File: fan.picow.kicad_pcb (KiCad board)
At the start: 2 copper layers, 60.3 x 65.7 mm, 53 parts, among them J10 5v Input, J11 12v Input, J12 Temp DHT22, J2 Fan1 Conn, J3 Fan2 Conn, J4 Fan4 Conn, J5 Fan3 Conn, J6 Buzz Conn, J7 OLED, J8 Relay Ctrl, J9 Relay Out, U1 PicoW

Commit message: pop stashed changes
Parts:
- removed J10: 5v Input, Connector_PinHeader_2.54mm:PinHeader_1x02_P2.54mm_Vertical
- removed J11: 12v Input, Connector_PinHeader_2.54mm:PinHeader_1x02_P2.54mm_Vertical
- removed J6: Buzz Conn, Connector_PinHeader_2.54mm:PinHeader_1x03_P2.54mm_Vertical
- removed J8: Relay Ctrl, Connector_PinHeader_2.54mm:PinHeader_1x03_P2.54mm_Vertical
- removed J9: Relay Out, Connector_PinHeader_2.54mm:PinHeader_1x03_P2.54mm_Vertical
- removed JP1: NO/NC Selector, Connector_PinHeader_2.54mm:PinHeader_1x03_P2.54mm_Vertical
- added C10: 0.1uF, Capacitor_SMD:C_0603_1608Metric_Pad1.08x0.95mm_HandSolder, F.Cu at (130.6, 103.1)
- added C11: 10uF, footprints descargados:CL21A106KOQNNNE, F.Cu at (165.4, 65.3)
- added C7: 10pF, Capacitor_SMD:C_0603_1608Metric_Pad1.08x0.95mm_HandSolder, F.Cu at (170.9, 65.3)
- added C8: 1uF, Capacitor_SMD:C_0603_1608Metric_Pad1.08x0.95mm_HandSolder, F.Cu at (168.4, 81.0)
- added D10: 12V, digikey-footprints:0805, F.Cu at (165.4, 89.4)
- added F1: Polyfuse 0.5A, Fuse:Fuse_1206_3216Metric_Pad1.42x1.75mm_HandSolder, F.Cu at (170.9, 62.0)
- added J1: 12v Input, Connector_PinHeader_2.54mm:PinHeader_1x02_P2.54mm_Vertical, F.Cu at (180.7, 82.9)
- added LS1: CMT-7525-80-SMT-TR, footprints descargados:XDCR_CMT-7525-80-SMT-TR, F.Cu at (139.7, 99.1)
- added Q1: AOD4184A, footprints descargados:DPAK228P994X240-4N, F.Cu at (161.8, 104.4)
- added Q2: BSS138, Package_TO_SOT_SMD:SOT-23, F.Cu at (147.3, 96.8)
- added R21: 160k, Resistor_SMD:R_0603_1608Metric_Pad0.98x0.95mm_HandSolder, F.Cu at (165.4, 69.6)
- added R22: 49.9k, Resistor_SMD:R_0603_1608Metric_Pad0.98x0.95mm_HandSolder, F.Cu at (171.9, 89.4)
- added R23: 1k, Resistor_SMD:R_0603_1608Metric_Pad0.98x0.95mm_HandSolder, F.Cu at (152.9, 100.8)
- added SW1: EG1257, footprints descargados:EG1257, F.Cu at (138.0, 108.0)
- added TP1: 5V, TestPoint:TestPoint_Pad_D1.5mm, F.Cu at (165.1, 62.0)
- added TP3: 12V, TestPoint:TestPoint_Pad_D1.5mm, F.Cu at (169.7, 95.0)
- added U2: TLV76701, footprints descargados:TLV76701DGNR, F.Cu at (168.2, 75.8)
- C2: value 0.1uF -> 10uF; footprint Capacitor_SMD:C_0603_1608Metric_Pad1.08x0.95mm_HandSolder -> footprints descargados:CL21A106KOQNNNE
- D1: value LED 12VF -> 12VF; footprint LED_SMD:LED_0805_2012Metric_Pad1.15x1.40mm_HandSolder -> digikey-footprints:0805
- D2, D3, D5, D6: footprint Diode_SMD:D_SMA_Handsoldering -> Diode_SMD:D_SOD-123
- D4: value LED 12V -> 5V; footprint LED_SMD:LED_0805_2012Metric_Pad1.15x1.40mm_HandSolder -> digikey-footprints:0805
- D7: value LED 3V3 -> 3V3; footprint LED_SMD:LED_0805_2012Metric_Pad1.15x1.40mm_HandSolder -> digikey-footprints:0805
- D8: value LED 5V -> ES1D; footprint LED_SMD:LED_0805_2012Metric_Pad1.15x1.40mm_HandSolder -> Diode_SMD:D_1206_3216Metric_Pad1.42x1.75mm_HandSolder
- D9: value 1N5819 -> CDBW140-G; footprint Diode_SMD:D_SMA_Handsoldering -> Diode_SMD:D_SOD-123F
- J12: value Temp DHT22 -> DHT22
- J2: value Fan1 Conn -> Fan1
- J3: value Fan2 Conn -> Fan2
- J4: value Fan4 Conn -> Fan4
- J5: value Fan3 Conn -> Fan3
- R16: value 10K -> 820k
- R8: value 49.9K -> 10k
- TP2: value TestP 3V3 -> 3V3
- moved R1 61.6 mm to (124.5, 46.5), turned to 180 degrees
- moved D1 55.0 mm to (130.0, 46.5), turned to 180 degrees
- moved D4 28.2 mm to (165.4, 56.9), turned to 180 degrees
- moved R8 25.1 mm to (170.9, 56.9), turned to 180 degrees
- moved R15 23.1 mm to (171.4, 52.7)
- moved D8 22.3 mm to (171.4, 84.8)
- moved D7 18.3 mm to (165.3, 52.8)
- moved C6 15.8 mm to (170.2, 44.7)
- moved C5 11.9 mm to (130.0, 50.3)
- moved C4 11.6 mm to (130.3, 62.7)
- moved C3 10.7 mm to (130.3, 75.7)
- moved J12 10.6 mm to (180.8, 56.6)
- moved J7 10.6 mm to (180.9, 68.2)
- moved C1 10.0 mm to (130.6, 88.4)
- moved H3 8.41 mm to (178.8, 106.9)
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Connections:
- C1 pad 2: GND -> /GNDFAN
- C2 pad 1: /12V -> Net-(C2-Pad1)
- C3 pad 2: GND -> /GNDFAN
- C4 pad 2: GND -> /GNDFAN
- C5 pad 2: GND -> /GNDFAN
- D1 pad 1: Net-(D1-Pad1) -> /12V
- D1 pad 2: /12VFAN -> Net-(D1-Pad2)
- D2 pad 1: Net-(D2-Pad1) -> /TACHM1
- D2 pad 2: /TACHM1 -> Net-(D2-Pad2)
- D3 pad 1: Net-(D3-Pad1) -> /TACHM2
- D3 pad 2: /TACHM2 -> Net-(D3-Pad2)
- D4 pad 2: /12V -> GND
- D5 pad 1: Net-(D5-Pad1) -> /TACHM3
- D5 pad 2: /TACHM3 -> Net-(D5-Pad2)
- D6 pad 1: Net-(D6-Pad1) -> /TACHM4
- D6 pad 2: /TACHM4 -> Net-(D6-Pad2)
- D7 pad 1: Net-(D7-Pad1) -> /3V3
- D7 pad 2: /3V3 -> Net-(D7-Pad2)
- D8 pad 1: Net-(D8-Pad1) -> Net-(C2-Pad1)
- D8 pad 2: /VSYS -> /12V
- J2 pad 1: GND -> /GNDFAN
- J2 pad 2: /12VFAN -> /12V
- J3 pad 1: GND -> /GNDFAN
- J3 pad 2: /12VFAN -> /12V
- J4 pad 1: GND -> /GNDFAN
- J4 pad 2: /12VFAN -> /12V
- J5 pad 1: GND -> /GNDFAN
- J5 pad 2: /12VFAN -> /12V
- R1 pad 1: Net-(D1-Pad1) -> Net-(D1-Pad2)
- R1 pad 2: GND -> /GNDFAN
- R10 pad 2: Net-(D5-Pad1) -> Net-(D5-Pad2)
- R11 pad 1: Net-(D5-Pad1) -> Net-(D5-Pad2)
- R11 pad 2: GND -> /GNDFAN
- R12 pad 1: /12VFAN -> /12V
- R13 pad 2: Net-(D6-Pad1) -> Net-(D6-Pad2)
- R14 pad 1: Net-(D6-Pad1) -> Net-(D6-Pad2)
- R14 pad 2: GND -> /GNDFAN
- R15 pad 1: Net-(D7-Pad1) -> Net-(D7-Pad2)
- R16 pad 1: Net-(D8-Pad1) -> Net-(C11-Pad1)
- R16 pad 2: GND -> Net-(C7-Pad2)
- R2 pad 1: /12VFAN -> /12V
- R3 pad 2: Net-(D2-Pad1) -> Net-(D2-Pad2)
- R4 pad 1: Net-(D2-Pad1) -> Net-(D2-Pad2)
- R4 pad 2: GND -> /GNDFAN
- R5 pad 1: /12VFAN -> /12V
- R6 pad 2: Net-(D3-Pad1) -> Net-(D3-Pad2)
- R7 pad 1: Net-(D3-Pad1) -> Net-(D3-Pad2)
- R7 pad 2: GND -> /GNDFAN
- R8 pad 1: Net-(D4-Pad1) -> /5V
- R8 pad 2: GND -> Net-(D4-Pad1)
- R9 pad 1: /12VFAN -> /12V
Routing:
- net /GNDFAN: track 0.00 -> 171.3 mm, vias 0 -> 1
- net /12VFAN: track 151.7 -> 0.00 mm
- net /12V: track 45.3 -> 194.0 mm, vias 2 -> 1
- net GND: track 68.5 -> 132.1 mm, vias 9 -> 2
- net /BUZZ: track 15.3 -> 48.5 mm
- net /3V3: track 136.8 -> 115.1 mm, vias 4 -> 0
- net /5V: track 9.74 -> 31.3 mm, vias 0 -> 2
- net Net-(C11-Pad1): track 0.00 -> 18.3 mm
- net /conectores/NCLOSED: track 16.2 -> 0.00 mm
- net Net-(C2-Pad1): track 0.00 -> 14.7 mm
- net Net-(C7-Pad2): track 0.00 -> 12.7 mm
- net /VSYS: track 29.5 -> 17.3 mm
- net Net-(Q1-Pad1): track 0.00 -> 12.1 mm
- net Net-(D2-Pad2): track 0.00 -> 11.1 mm
- net /TEMPHUM: track 18.7 -> 29.7 mm
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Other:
- board size 60.3 x 65.7 mm -> 73.4 x 70.5 mm
- board text added: "0.2000 mm / 0.0000 mm"
- board text added: "0.3000 mm"
- board text added: "1.6000 mm"
- board text added: "2"
- board text added: "60.2996 mm x 65.6844 mm"
- board text added: "BOARD CHARACTERISTICS"
- board text added: "Board Thickness:"
- board text added: "Board overall dimensions:"
- board text added: "Castellated pads:"
- board text added: "Copper Finish:"
- board text added: "Copper Layer Count:"
- board text added: "Edge card connectors:"
- board text added: "Falta: - Graficos detras - Version de la placa - Iniciales - Tamaño de la placa (para caja standard) y posicion agujeros - Redondear los bordes (cambiar rectangulo por lineas) - Tamaños de los componentes"
- board text added: "Fan Controller v0.1 Based on RaspberryPi PicoW MCU"
- board text added: "Impedance Control:"
- board text added: "Min hole diameter:"
- board text added: "Min track/spacing:"
- board text added: "No"
- board text added: "None"
- board text added: "Plated Board Edge:"
- board text added: "by Jaime Botella jimbotel@gmail.com 2022/11"
- board text removed: "12VF"
- board text removed: "5V"
- board text removed: "Falta: - Graficos detras - Version de la placa - Iniciales - Validar valores Rs de LEDs - Tamaños de los componentes"
- board text removed: "IN"
- board text removed: "NCLSD"
- board text removed: "NOPEN"
- board text removed: "RELC"

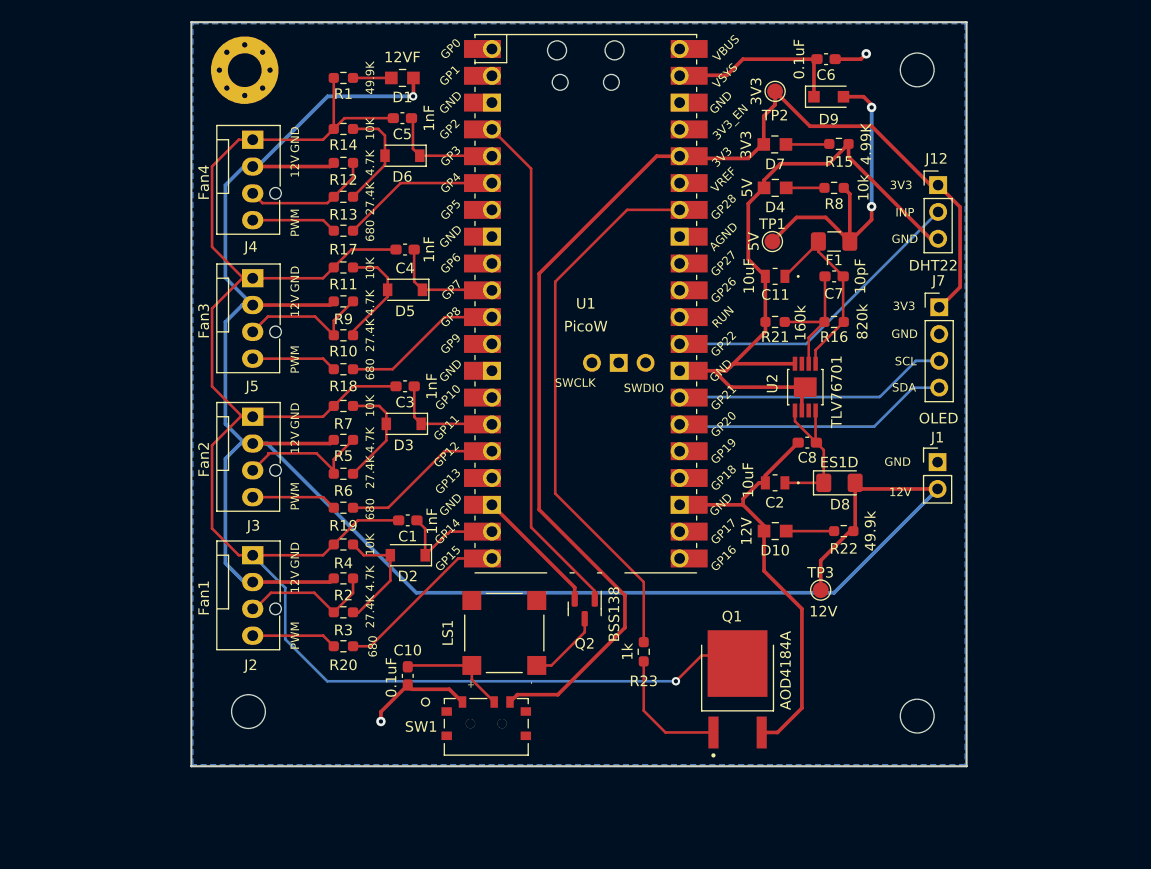
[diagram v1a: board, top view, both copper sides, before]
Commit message: add GNDFAN net to Power netclass
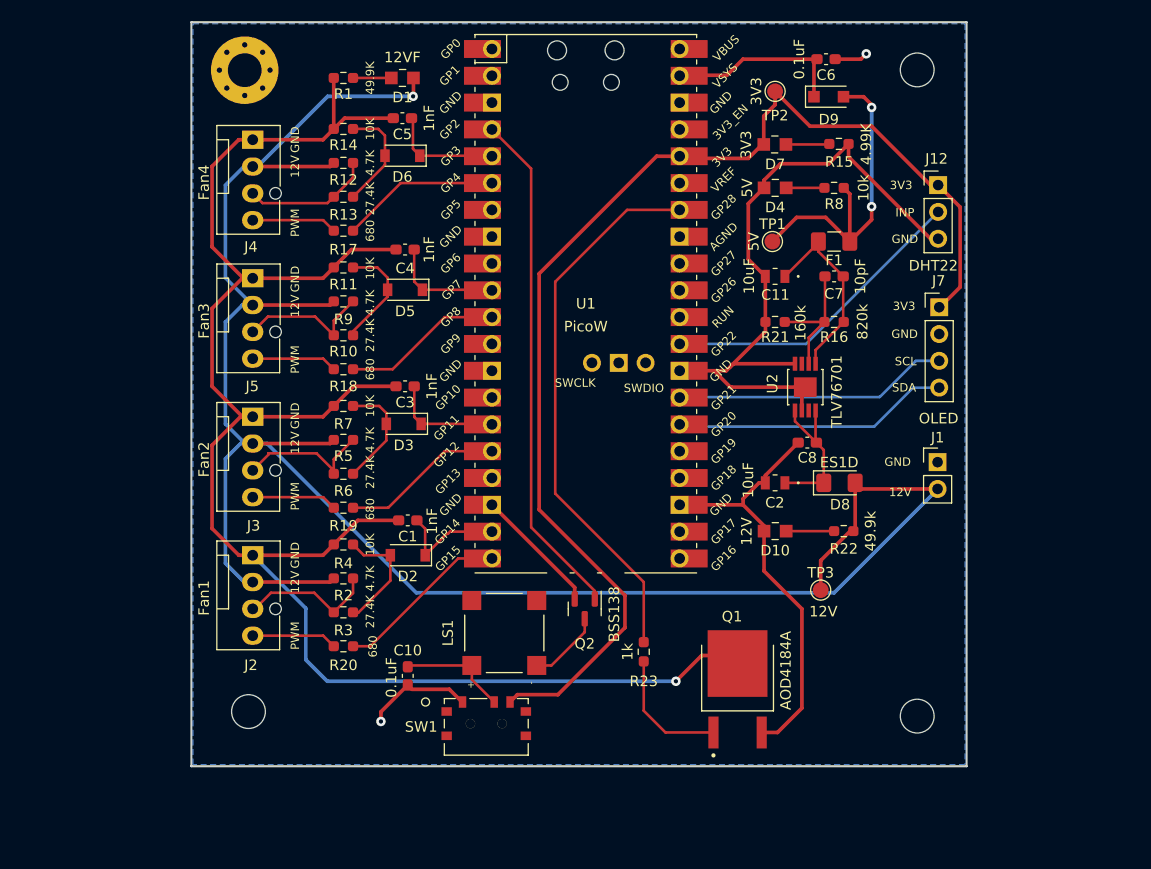
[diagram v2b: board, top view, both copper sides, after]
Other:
- board text added: "Falta: - Tamaño de la placa (para caja standard) y posicion agujeros - Redondear los bordes (cambiar rectangulo por lineas)"
- board text removed: "0.2000 mm / 0.0000 mm"
- board text removed: "0.3000 mm"
- board text removed: "1.6000 mm"
- board text removed: "2"
- board text removed: "60.2996 mm x 65.6844 mm"
- board text removed: "BOARD CHARACTERISTICS"
- board text removed: "Board Thickness:"
- board text removed: "Board overall dimensions:"
- board text removed: "Castellated pads:"
- board text removed: "Copper Finish:"
- board text removed: "Copper Layer Count:"
- board text removed: "Edge card connectors:"
- board text removed: "Falta: - Graficos detras - Version de la placa - Iniciales - Tamaño de la placa (para caja standard) y posicion agujeros - Redondear los bordes (cambiar rectangulo por lineas) - Tamaños de los componentes"
- board text removed: "Impedance Control:"
- board text removed: "Min hole diameter:"
- board text removed: "Min track/spacing:"
- board text removed: "No"
- board text removed: "None"
- board text removed: "Plated Board Edge:"

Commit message: edit some footprints to give more room to the pads
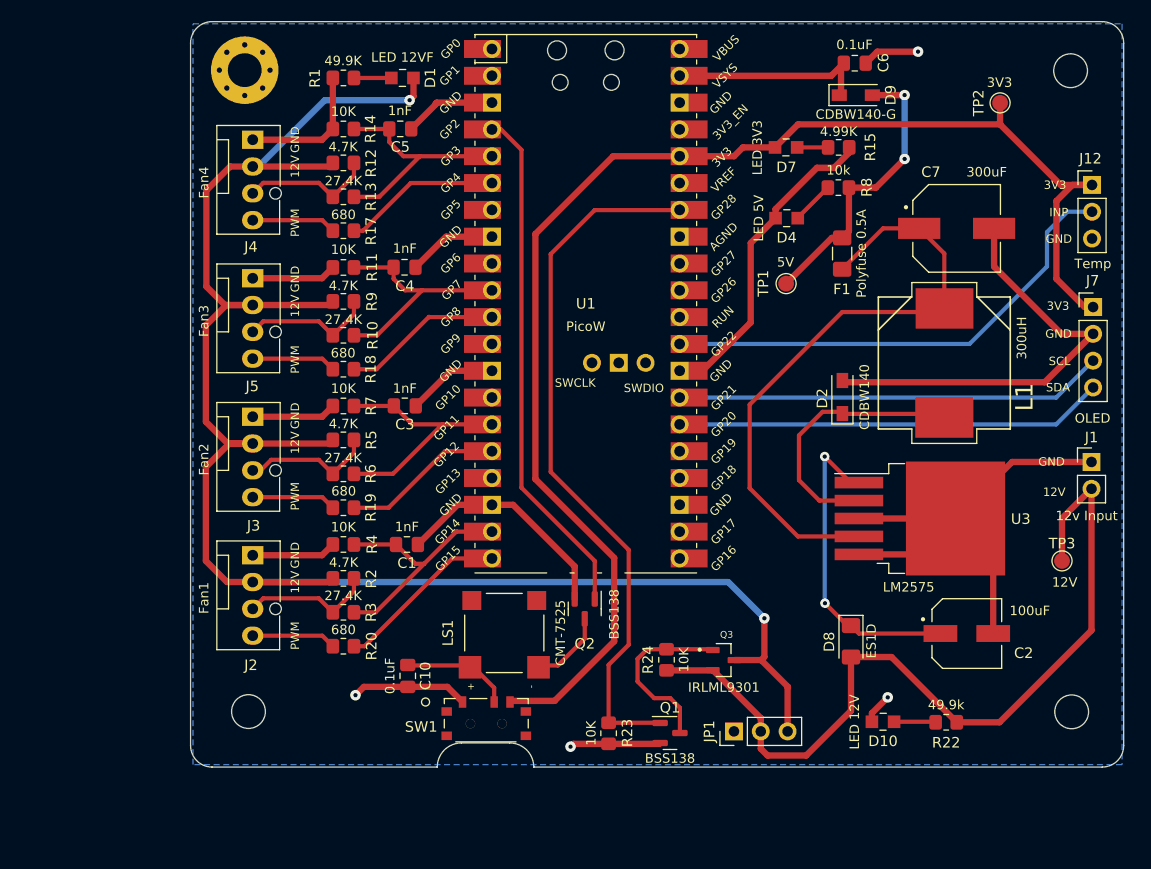
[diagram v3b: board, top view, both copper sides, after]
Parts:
- removed C11: 10uF, footprints descargados:CL21A106KOQNNNE
- removed C8: 1uF, Capacitor_SMD:C_0603_1608Metric_Pad1.08x0.95mm_HandSolder
- removed D3, D5, D6: 1N4148, Diode_SMD:D_SOD-123
- removed R16: 820k, Resistor_SMD:R_0603_1608Metric_Pad0.98x0.95mm_HandSolder
- removed R21: 160k, Resistor_SMD:R_0603_1608Metric_Pad0.98x0.95mm_HandSolder
- removed U2: TLV76701, footprints descargados:TLV76701DGNR
- added JP1: Jumper_3_Bridged12, Connector_PinHeader_2.54mm:PinHeader_1x03_P2.54mm_Vertical, F.Cu at (161.5, 108.4)
- added L1: 300uH, footprints descargados:DR127-331_INDM125125X800N, F.Cu at (181.4, 73.5)
- added Q3: IRLML9301, footprints descargados:IRLML9301TRPBF.SOT95P237X112-3N, F.Cu at (160.5, 101.6)
- added R24: 10K, Resistor_SMD:R_0805_2012Metric_Pad1.20x1.40mm_HandSolder, F.Cu at (155.1, 101.6)
- added U3: LM2575, Package_TO_SOT_SMD:TO-263-5_TabPin3, F.Cu at (179.1, 88.2)
- C1, C10, C3, C4, C5, C6: footprint Capacitor_SMD:C_0603_1608Metric_Pad1.08x0.95mm_HandSolder -> Capacitor_SMD:C_0805_2012Metric_Pad1.18x1.45mm_HandSolder
- C2: value 10uF -> 100uF; footprint footprints descargados:CL21A106KOQNNNE -> footprints descargados:CAP_EEEHA1V101XP
- C7: value 10pF -> 300uF; footprint Capacitor_SMD:C_0603_1608Metric_Pad1.08x0.95mm_HandSolder -> footprints descargados:CAP_EEEFT1V331AP
- D1: value 12VF -> LED 12VF
- D10: value 12V -> LED 12V
- D2: value 1N4148 -> CDBW140; footprint Diode_SMD:D_SOD-123 -> Diode_SMD:D_SOD-123F
- D4: value 5V -> LED 5V
- D7: value 3V3 -> LED 3V3
- J12: value DHT22 -> Temp
- LS1: value CMT-7525-80-SMT-TR -> CMT-7525
- Q1: value AOD4184A -> BSS138; footprint footprints descargados:DPAK228P994X240-4N -> Package_TO_SOT_SMD:SOT-23
- R1, R10, R11, R12, R13, R14, R15, R17, R18, R19, R2, R20, R22, R3, R4, R5, R6, R7, R8, R9: footprint Resistor_SMD:R_0603_1608Metric_Pad0.98x0.95mm_HandSolder -> Resistor_SMD:R_0805_2012Metric_Pad1.20x1.40mm_HandSolder
- R23: value 1k -> 10K; footprint Resistor_SMD:R_0603_1608Metric_Pad0.98x0.95mm_HandSolder -> Resistor_SMD:R_0805_2012Metric_Pad1.20x1.40mm_HandSolder
- moved D2 43.8 mm to (171.7, 76.7), turned to 90 degrees
- moved C2 23.1 mm to (183.5, 99.1), turned to 0 degrees
- moved TP3 23.0 mm to (192.5, 92.2)
- moved TP2 21.3 mm to (186.7, 48.8), turned to -90 degrees
- moved D10 20.8 mm to (175.6, 107.5)
- moved R22 20.5 mm to (181.6, 107.5)
- moved D8 15.1 mm to (172.5, 99.8), turned to -90 degrees
- moved H3 14.6 mm to (193.4, 106.5)
- moved J1 14.6 mm to (195.3, 82.9)
- moved J12 14.6 mm to (195.4, 56.6)
- moved J7 14.6 mm to (195.5, 68.2)
- moved H1 14.5 mm to (193.3, 45.8)
- moved C7 12.5 mm to (182.5, 60.7), turned to 0 degrees
- moved R23 8.41 mm to (149.6, 108.6)
- moved Q1 7.62 mm to (155.4, 108.5)
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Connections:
- C1 pad 2: /GNDFAN -> GND
- C3 pad 2: /GNDFAN -> GND
- C4 pad 2: /GNDFAN -> GND
- C5 pad 2: /GNDFAN -> GND
- C7 pad 2: Net-(C7-Pad2) -> GND
- D1 pad 1: /12V -> /12VF
- D2 pad 1: /TACHM1 -> Net-(D2-Pad1)
- D2 pad 2: Net-(D2-Pad2) -> GND
- J2 pad 1: /GNDFAN -> GND
- J2 pad 2: /12V -> /12VF
- J3 pad 1: /GNDFAN -> GND
- J3 pad 2: /12V -> /12VF
- J4 pad 1: /GNDFAN -> GND
- J4 pad 2: /12V -> /12VF
- J5 pad 1: /GNDFAN -> GND
- J5 pad 2: /12V -> /12VF
- Q1 pad 1: Net-(Q1-Pad1) -> /RELC
- Q1 pad 3: GND -> Net-(Q1-Pad3)
- R1 pad 2: /GNDFAN -> GND
- R10 pad 2: Net-(D5-Pad2) -> /TACHM3
- R11 pad 1: Net-(D5-Pad2) -> /TACHM3
- R11 pad 2: /GNDFAN -> GND
- R12 pad 1: /12V -> /12VF
- R13 pad 2: Net-(D6-Pad2) -> /TACHM4
- R14 pad 1: Net-(D6-Pad2) -> /TACHM4
- R14 pad 2: /GNDFAN -> GND
- R2 pad 1: /12V -> /12VF
- R23 pad 2: Net-(Q1-Pad1) -> GND
- R3 pad 2: Net-(D2-Pad2) -> /TACHM1
- R4 pad 1: Net-(D2-Pad2) -> /TACHM1
- R4 pad 2: /GNDFAN -> GND
- R5 pad 1: /12V -> /12VF
- R6 pad 2: Net-(D3-Pad2) -> /TACHM2
- R7 pad 1: Net-(D3-Pad2) -> /TACHM2
- R7 pad 2: /GNDFAN -> GND
- R9 pad 1: /12V -> /12VF
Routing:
- net /12VF: track 0.00 -> 173.7 mm, vias 0 -> 2
- net /GNDFAN: track 171.3 -> 0.00 mm, vias 1 -> 0
- net /12V: track 194.0 -> 79.7 mm, vias 1 -> 0
- net GND: track 132.1 -> 231.1 mm, vias 2 -> 4
- net Net-(C7-Pad1): track 18.3 -> 60.1 mm
- net Net-(D2-Pad1): track 0.00 -> 25.5 mm
- net Net-(Q1-Pad3): track 0.00 -> 17.1 mm
- net /TEMPHUM: track 29.7 -> 46.2 mm
- net /3V3: track 115.1 -> 131.3 mm
- net Net-(C2-Pad1): track 14.7 -> 30.3 mm, vias 0 -> 2
- net /RELC: track 52.2 -> 67.1 mm
- net /SCL: track 26.0 -> 40.6 mm
- net /SDA: track 26.2 -> 40.6 mm
- net /TACHM2: track 10.6 -> 24.1 mm
- net /TACHM1: track 10.9 -> 23.7 mm
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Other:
- board size 73.4 x 70.5 mm -> 88.4 x 70.6 mm
- board text added: "Fan Controller v0.2 Based on RaspberryPi PicoW MCU"
- board text added: "by Jaime Botella jimbotel@gmail.com 2023/03"
- board text removed: "Fan Controller v0.1 Based on RaspberryPi PicoW MCU"
- board text removed: "by Jaime Botella jimbotel@gmail.com 2022/11"

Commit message: resize pcb to match 100mm length
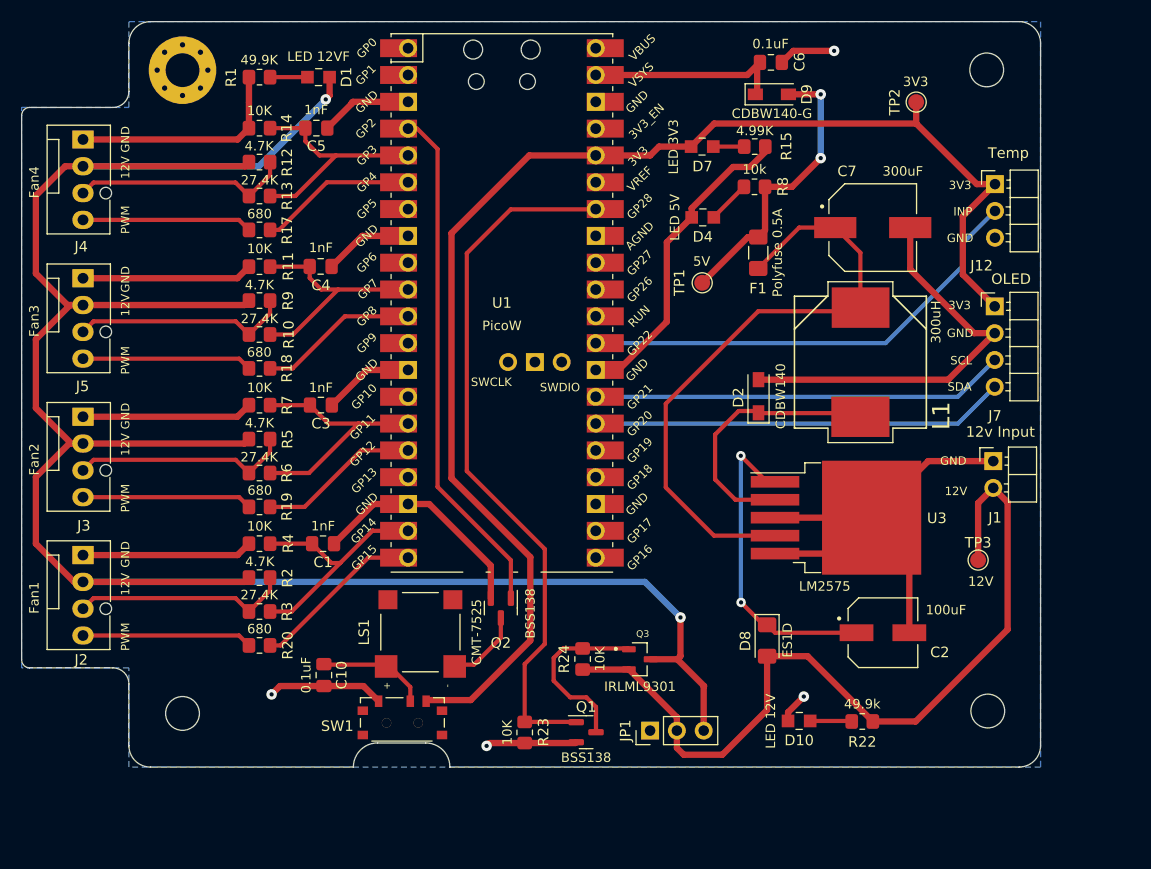
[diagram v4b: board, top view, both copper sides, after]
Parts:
- J1: footprint Connector_PinHeader_2.54mm:PinHeader_1x02_P2.54mm_Vertical -> Connector_PinHeader_2.54mm:PinHeader_1x02_P2.54mm_Horizontal
- J12: footprint Connector_PinHeader_2.54mm:PinHeader_1x03_P2.54mm_Vertical -> Connector_PinHeader_2.54mm:PinHeader_1x03_P2.54mm_Horizontal
- J7: footprint Connector_PinHeader_2.54mm:PinHeader_1x04_P2.54mm_Vertical -> Connector_PinHeader_2.54mm:PinHeader_1x04_P2.54mm_Horizontal
- moved J4 16.1 mm to (99.8, 52.3)
- moved J2 16.1 mm to (99.8, 91.7)
- moved J3 16.1 mm to (99.8, 78.6)
- moved J5 16.1 mm to (99.8, 65.5)
- moved J7 9.32 mm to (186.2, 68.1)
- moved J1 9.31 mm to (186.0, 82.8)
- moved J12 9.20 mm to (186.2, 56.5)
- moved C1 7.95 mm to (122.5, 90.6)
- moved C10 7.95 mm to (122.6, 103.0)
- moved C4 7.95 mm to (122.3, 64.3)
- moved C3 7.95 mm to (122.3, 77.5)
- moved C6 7.95 mm to (165.0, 45.0)
- moved C7 7.95 mm to (174.6, 60.7)
- moved D1 7.95 mm to (122.1, 46.4)
- moved D10 7.95 mm to (167.6, 107.4)
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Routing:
- net /12VF: track 173.7 -> 218.8 mm
- net GND: track 231.1 -> 259.7 mm
- net /TACH2: track 11.8 -> 20.7 mm
- net /PWMO4: track 8.00 -> 16.1 mm
- net /TACH4: track 12.6 -> 20.7 mm
- net /PWMO1: track 8.00 -> 16.1 mm
- net /TACH1: track 12.6 -> 20.7 mm
- net /PWMO3: track 8.00 -> 16.1 mm
- net /PWMO2: track 8.00 -> 16.1 mm
- net /TACH3: track 12.6 -> 20.7 mm
- net /3V3: track 131.3 -> 128.2 mm
- net /TEMPHUM: track 46.2 -> 44.3 mm
- net /SCL: track 40.6 -> 39.2 mm
- net /SDA: track 40.6 -> 39.2 mm
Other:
- board size 88.4 x 70.6 mm -> 96.5 x 70.6 mm
